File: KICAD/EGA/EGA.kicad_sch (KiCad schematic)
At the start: 39 parts, among them J1 12V, J10 TEST_TRIG, J2 HC-SR04, J3 LCD 20x4, J4 RTC, J5 TEST_PWM, J6 FAN_12V_PWM_3.3V, J7 UART, J8 TEST_RPM, J9 TEST_ECHO, SW1 PAGINA, SW2 RESET, U1 LM7805_TO220, U2 LM317_TO-220, U3 Pico

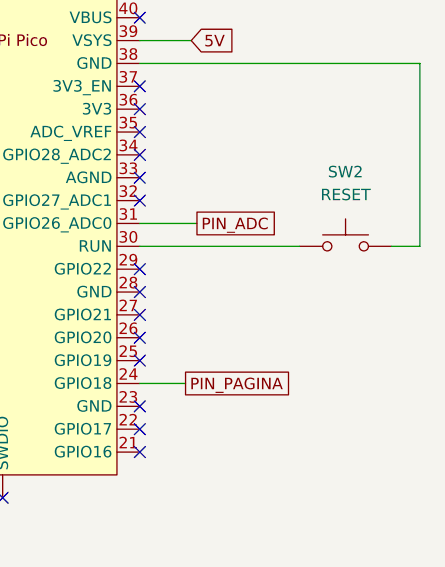
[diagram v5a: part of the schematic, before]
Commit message: Cambios en Kicad, adicion de Cuentionario, Adicion de informe
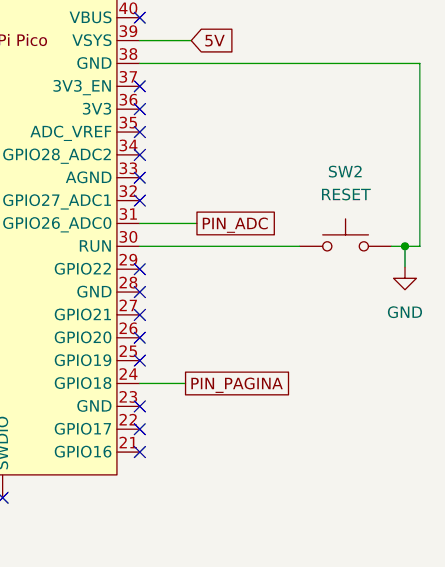
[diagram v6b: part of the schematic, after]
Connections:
- net GND: now also SW2.2, U3.38 (GND)
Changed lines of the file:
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@@
 	)
 	(junction
+		(at 277.114 127)
+		(diameter 0)
+		(color 0 0 0 0)
+	)
+	(junction
 		(at 38.862 42.418)
 		(diameter 0)
@@
 	(wire
 		(pts
+			(xy 277.114 127) (xy 277.114 129.286)
+		)
+		(stroke
+			(width 0)
+			(type default)
+		)
+	)
+	(wire
+		(pts
 			(xy 51.054 136.652) (xy 51.054 142.24)
 		)
@@
 	(wire
 		(pts
+			(xy 277.114 127) (xy 278.765 127)
+		)
+		(stroke
+			(width 0)
+			(type default)
+		)
+	)
+	(wire
+		(pts
 			(xy 50.038 42.418) (xy 43.942 42.418)
 		)
@@
 	(wire
 		(pts
-			(xy 275.59 127) (xy 278.765 127)
+			(xy 275.59 127) (xy 277.114 127)
 		)
 		(stroke
@@
 					(unit 1)
 				)
+			)
+		)
+	)
+	(symbol
+		(lib_id "power:GND")
+		(at 277.114 129.286 0)
+		(unit 1)
+		(exclude_from_sim no)
+		(in_bom yes)
+		(on_board yes)
+		(dnp no)
+		(fields_autoplaced yes)
+		(property "Reference" "#PWR03"
+			(at 277.114 135.636 0)
+			(effects
+				(font
+					(size 1.27 1.27)
+				)
+				(hide yes)
+			)
+		)
+		(property "Value" "GND"
+			(at 277.114 134.366 0)
+			(effects
+				(font
+					(size 1.27 1.27)
+				)
+			)
+		)
+		(property "Footprint" ""
+			(at 277.114 129.286 0)
+			(effects
+				(font
+					(size 1.27 1.27)
+				)
+				(hide yes)
+			)
+		)
+		(property "Datasheet" ""
+			(at 277.114 129.286 0)
+			(effects
+				(font
+					(size 1.27 1.27)
+				)
+				(hide yes)
+			)
+		)
+		(property "Description" "Power symbol creates a global label with name \"GND\" , ground"
+			(at 277.114 129.286 0)
+			(effects
+				(font
+					(size 1.27 1.27)
+				)
+				(hide yes)
+			)
+		)
+		(pin "1"
+		)
+		(instances
+			(project "EGA"
+				(path "/1d57e6f0-0119-4d90-b16e-372a255001d1"
+					(reference "#PWR03")
+					(unit 1)
+				)

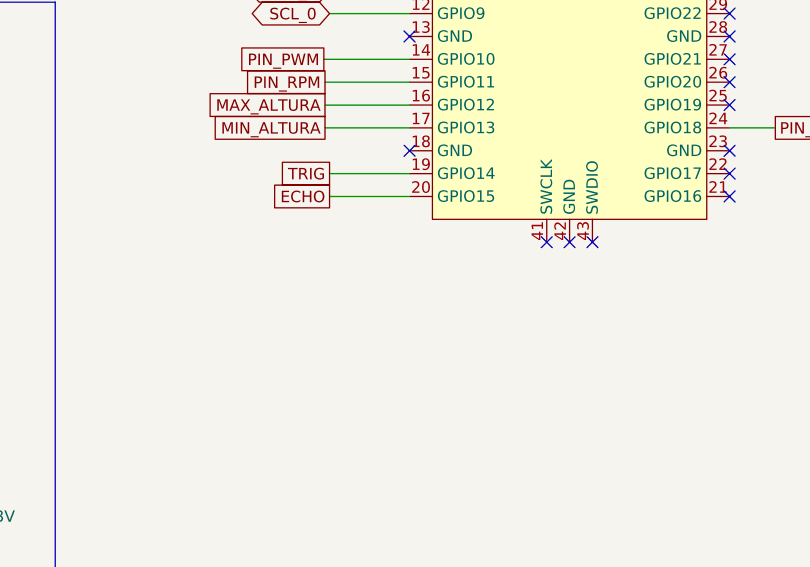
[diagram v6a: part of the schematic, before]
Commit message: Codigo bare metal PID, modificacion esquematico
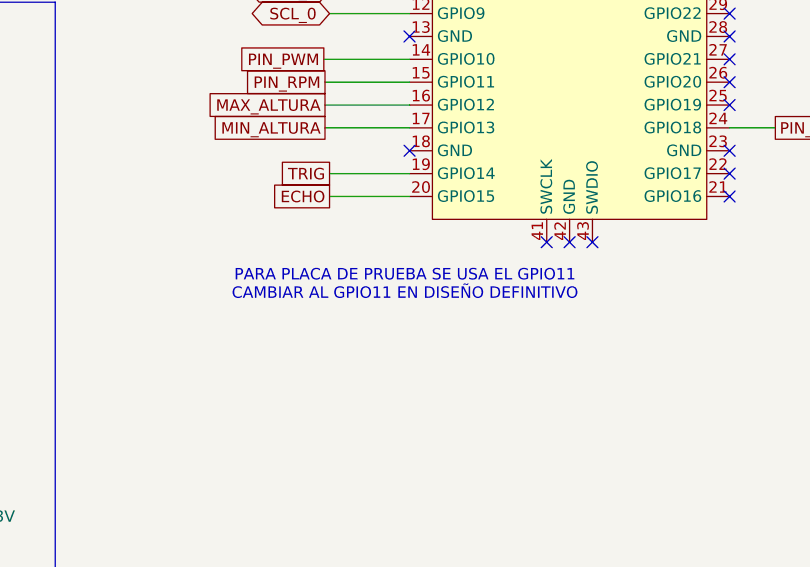
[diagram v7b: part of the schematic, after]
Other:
- note added: "PARA PLACA DE PRUEBA SE USA EL GPIO11 CAMBIAR AL GPIO11 EN DISEÑO DEFINITIVO"
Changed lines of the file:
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@@
+		)
+	)
+	(text "PARA PLACA DE PRUEBA SE USA EL GPIO11\nCAMBIAR AL GPIO11 EN DISEÑO DEFINITIVO\n\n"
+		(exclude_from_sim no)
+		(at 211.582 160.782 0)
+		(effects
+			(font
+				(size 1.27 1.27)
+			)
 		)
 	)

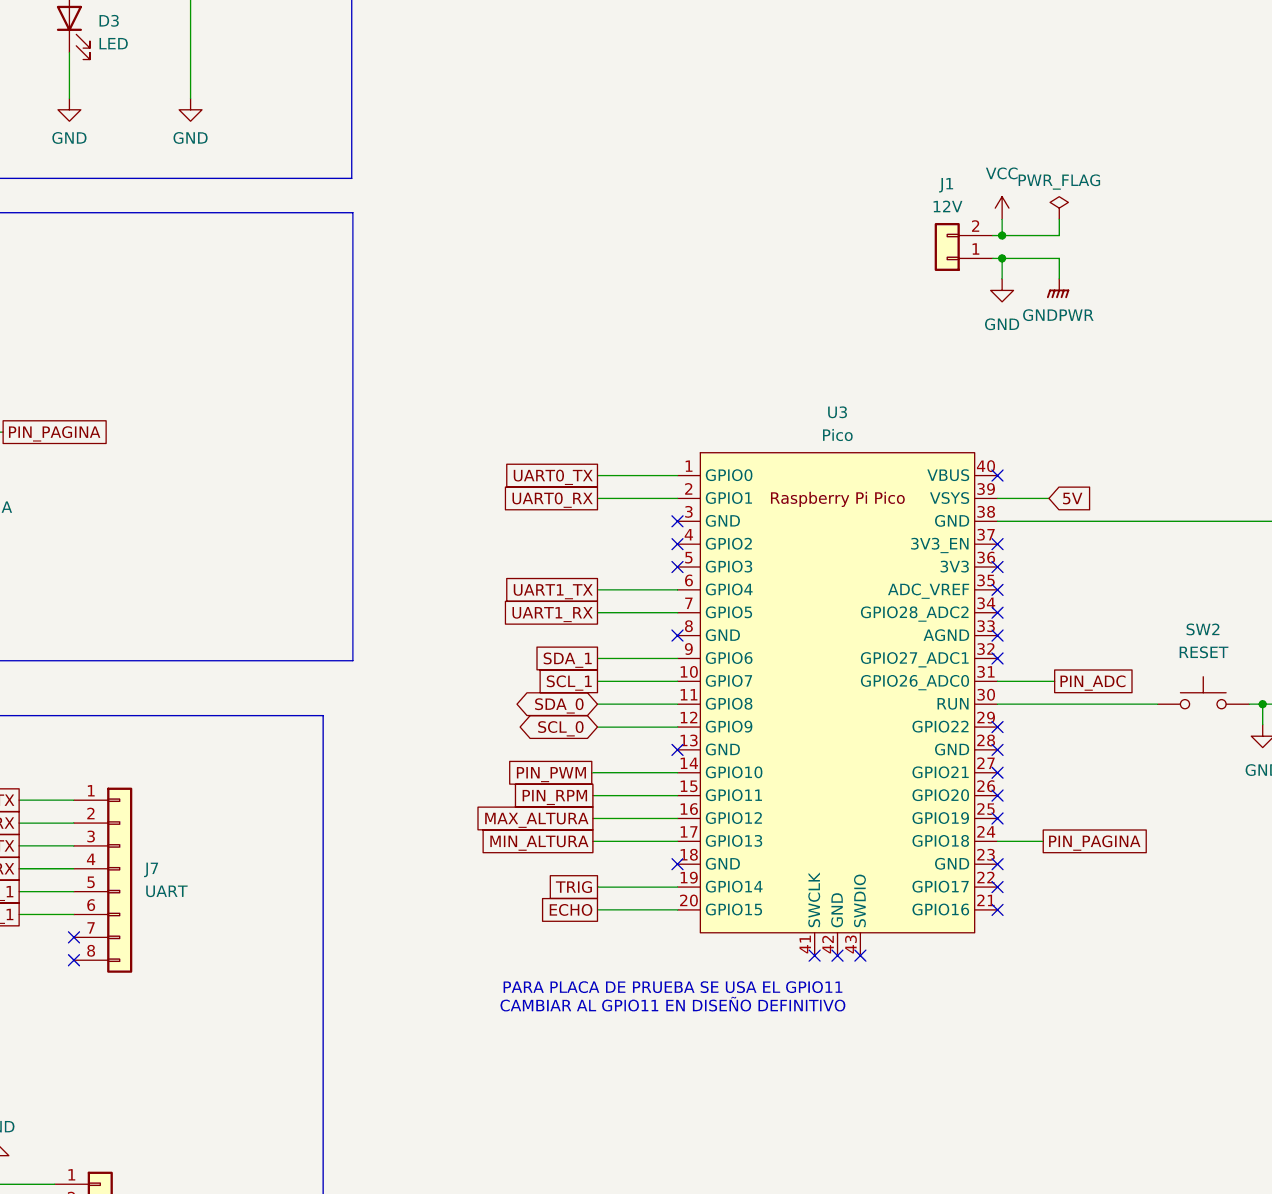
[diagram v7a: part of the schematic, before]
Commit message: Adicion en Informe, Adicion de Diagrama de tareas y conexiones, Ajuste de los K del PID, Adicion de modulo SD en KICAD
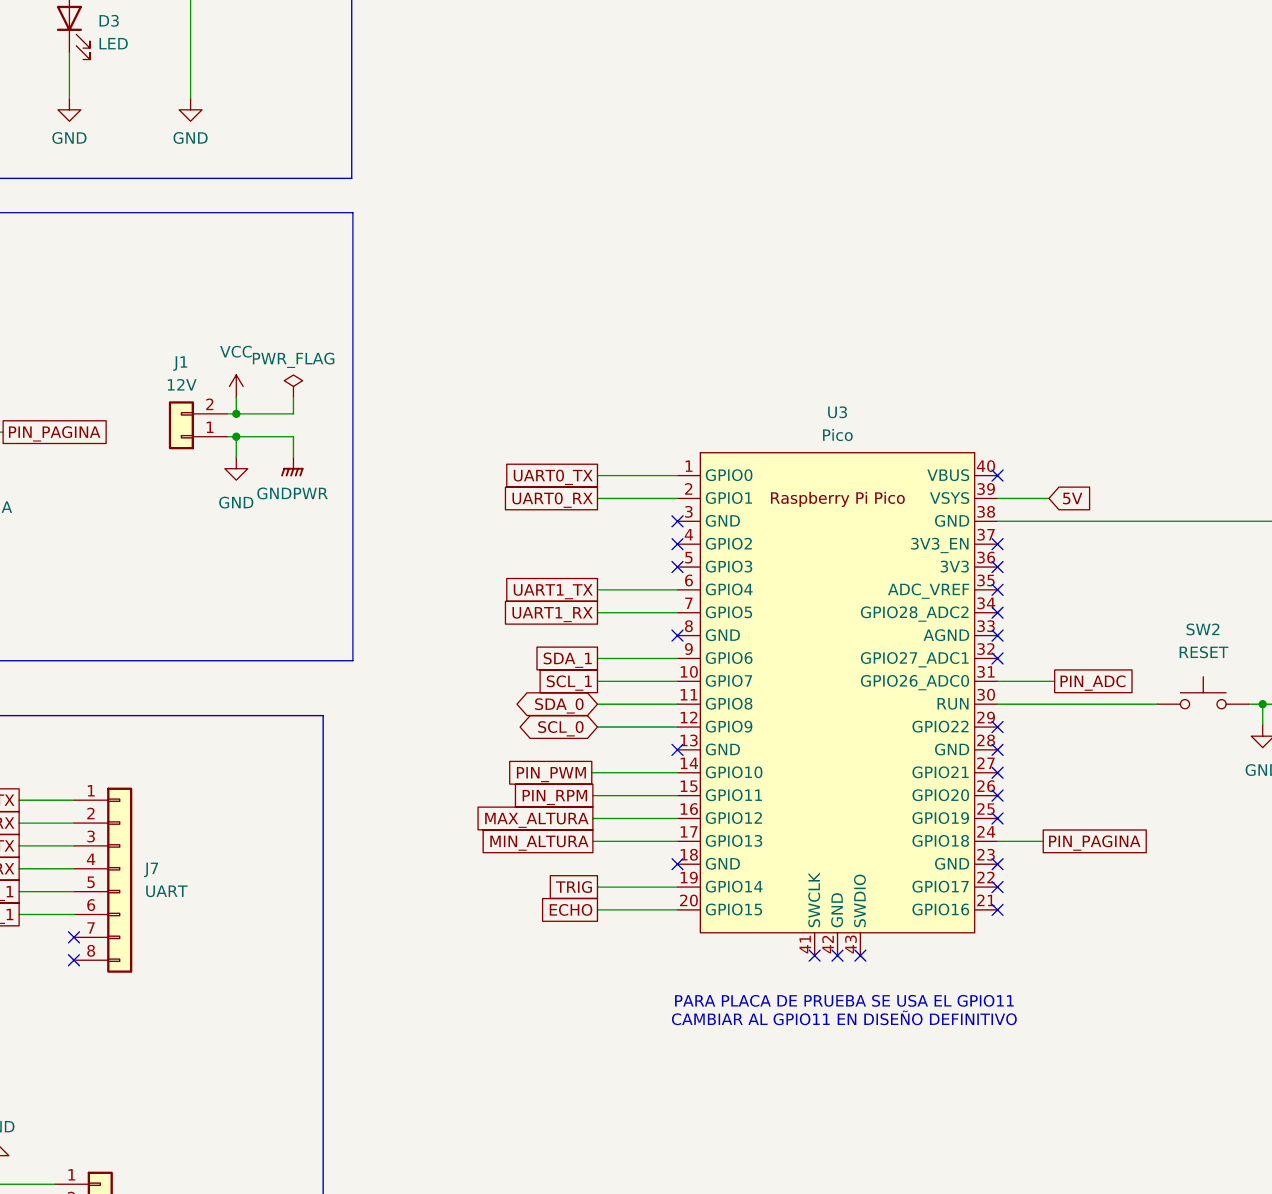
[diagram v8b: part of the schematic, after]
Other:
- moved on the sheet: J1
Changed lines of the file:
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@@
 	)
 	(junction
-		(at 248.158 77.47)
+		(at 163.068 97.282)
 		(diameter 0)
 		(color 0 0 0 0)
@@
 	)
 	(junction
-		(at 248.158 74.93)
+		(at 163.068 94.742)
 		(diameter 0)
 		(color 0 0 0 0)
@@
 	(wire
 		(pts
-			(xy 254.508 73.152) (xy 254.508 74.93)
+			(xy 169.418 92.964) (xy 169.418 94.742)
 		)
 		(stroke
@@
 	(wire
 		(pts
-			(xy 254.508 79.756) (xy 254.508 77.47)
+			(xy 169.418 99.568) (xy 169.418 97.282)
 		)
 		(stroke
@@
 	(wire
 		(pts
-			(xy 254.508 74.93) (xy 248.158 74.93)
+			(xy 169.418 94.742) (xy 163.068 94.742)
 		)
 		(stroke
@@
 	(wire
 		(pts
-			(xy 247.142 77.47) (xy 248.158 77.47)
+			(xy 162.052 97.282) (xy 163.068 97.282)
 		)
 		(stroke
@@
 	(wire
 		(pts
-			(xy 248.158 77.47) (xy 248.158 79.756)
+			(xy 163.068 97.282) (xy 163.068 99.568)
 		)
 		(stroke
@@
 	(wire
 		(pts
-			(xy 247.142 74.93) (xy 248.158 74.93)
+			(xy 162.052 94.742) (xy 163.068 94.742)
 		)
 		(stroke
@@
 	(wire
 		(pts
-			(xy 248.158 74.93) (xy 248.158 73.152)
+			(xy 163.068 94.742) (xy 163.068 92.964)
 		)
 		(stroke
@@
 	(wire
 		(pts
-			(xy 254.508 77.47) (xy 248.158 77.47)
+			(xy 169.418 97.282) (xy 163.068 97.282)
 		)
 		(stroke
@@
 	(text "PARA PLACA DE PRUEBA SE USA EL GPIO11\nCAMBIAR AL GPIO11 EN DISEÑO DEFINITIVO\n\n"
 		(exclude_from_sim no)
-		(at 211.582 160.782 0)
+		(at 230.632 162.306 0)
 		(effects
 			(font
@@
 	(symbol
 		(lib_id "power:PWR_FLAG")
-		(at 254.508 73.152 0)
+		(at 169.418 92.964 0)
 		(unit 1)
 		(exclude_from_sim no)
@@
 		(fields_autoplaced yes)
 		(property "Reference" "#FLG01"
-			(at 254.508 71.247 0)
+			(at 169.418 91.059 0)
 			(effects
 				(font
@@
 		)
 		(property "Value" "PWR_FLAG"
-			(at 254.508 68.834 0)
+			(at 169.418 88.646 0)
 			(effects
 				(font
@@
 		)
 		(property "Footprint" ""
-			(at 254.508 73.152 0)
+			(at 169.418 92.964 0)
 			(effects
 				(font
@@
 		)
 		(property "Datasheet" "~"
-			(at 254.508 73.152 0)
+			(at 169.418 92.964 0)
 			(effects
 				(font
@@
 		)
 		(property "Description" "Special symbol for telling ERC where power comes from"
-			(at 254.508 73.152 0)
+			(at 169.418 92.964 0)
 			(effects
 				(font
@@
 	(symbol
 		(lib_id "power:VCC")
-		(at 248.158 73.152 0)
+		(at 163.068 92.964 0)
 		(unit 1)
 		(exclude_from_sim no)
@@
 		(fields_autoplaced yes)
 		(property "Reference" "#PWR028"
-			(at 248.158 76.962 0)
+			(at 163.068 96.774 0)
 			(effects
 				(font
@@
 		)
 		(property "Value" "VCC"
-			(at 248.158 68.072 0)
+			(at 163.068 87.884 0)
 			(effects
 				(font
@@
 		)
 		(property "Footprint" ""
-			(at 248.158 73.152 0)
+			(at 163.068 92.964 0)
 			(effects
 				(font
@@
 		)
 		(property "Datasheet" ""
-			(at 248.158 73.152 0)
+			(at 163.068 92.964 0)
 			(effects
 				(font
@@
 		)
 		(property "Description" "Power symbol creates a global label with name \"VCC\""
-			(at 248.158 73.152 0)
+			(at 163.068 92.964 0)
 			(effects
 				(font
@@
 	(symbol
 		(lib_id "Connector_Generic:Conn_01x02")
-		(at 242.062 77.47 180)
+		(at 156.972 97.282 180)
 		(unit 1)
 		(exclude_from_sim no)
@@
 		(fields_autoplaced yes)
 		(property "Reference" "J1"
-			(at 242.062 69.215 0)
+			(at 156.972 89.027 0)
 			(effects
 				(font
@@
 		)
 		(property "Value" "12V"
-			(at 242.062 71.755 0)
+			(at 156.972 91.567 0)
 			(effects
 				(font
@@
 		)
 		(property "Footprint" "Connector_Molex:Molex_KK-254_AE-6410-02A_1x02_P2.54mm_Vertical"
-			(at 242.062 77.47 0)
+			(at 156.972 97.282 0)
 			(effects
 				(font
@@
 		)
 		(property "Datasheet" "~"
-			(at 242.062 77.47 0)
+			(at 156.972 97.282 0)
 			(effects
 				(font
@@
 		)
 		(property "Description" "Generic connector, single row, 01x02, script generated (kicad-library-utils/schlib/autogen/connector/)"
-			(at 242.062 77.47 0)
+			(at 156.972 97.282 0)
 			(effects
 				(font
@@
 	(symbol
 		(lib_id "power:GND")
-		(at 248.158 79.756 0)
+		(at 163.068 99.568 0)
 		(unit 1)
 		(exclude_from_sim no)
@@
 		(fields_autoplaced yes)
 		(property "Reference" "#PWR02"
-			(at 248.158 86.106 0)
+			(at 163.068 105.918 0)
 			(effects
 				(font
@@
 		)
 		(property "Value" "GND"
-			(at 248.158 84.836 0)
+			(at 163.068 104.648 0)
 			(effects
 				(font
@@
 		)
 		(property "Footprint" ""
-			(at 248.158 79.756 0)
+			(at 163.068 99.568 0)
 			(effects
 				(font
@@
 		)
 		(property "Datasheet" ""
-			(at 248.158 79.756 0)
+			(at 163.068 99.568 0)
 			(effects
 				(font
@@
 		)
 		(property "Description" "Power symbol creates a global label with name \"GND\" , ground"
-			(at 248.158 79.756 0)
+			(at 163.068 99.568 0)
 			(effects
 				(font
@@
 	(symbol
 		(lib_id "power:GNDPWR")
-		(at 254.508 79.756 0)
+		(at 169.418 99.568 0)
 		(unit 1)
 		(exclude_from_sim no)
@@
 		(fields_autoplaced yes)
 		(property "Reference" "#PWR029"
-			(at 254.508 84.836 0)
+			(at 169.418 104.648 0)
 			(effects
 				(font
@@
 		)
 		(property "Value" "GNDPWR"
-			(at 254.381 83.82 0)
+			(at 169.291 103.632 0)
 			(effects
 				(font
@@
 		)
 		(property "Footprint" ""
-			(at 254.508 81.026 0)
+			(at 169.418 100.838 0)
 			(effects
 				(font
@@
 		)
 		(property "Datasheet" ""
-			(at 254.508 81.026 0)
+			(at 169.418 100.838 0)
 			(effects
 				(font
@@
 		)
 		(property "Description" "Power symbol creates a global label with name \"GNDPWR\" , global ground"
-			(at 254.508 79.756 0)
+			(at 169.418 99.568 0)
 			(effects
 				(font
